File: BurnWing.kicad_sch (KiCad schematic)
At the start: 23 parts, among them J1 Molex_PicoBlade_53398-0471_1x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, J2 Molex_PicoBlade_53047-0610_1x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, J3 feather long, J4 feather short, U1 BTS3405GXUMA1, U3 AP63205WU-7

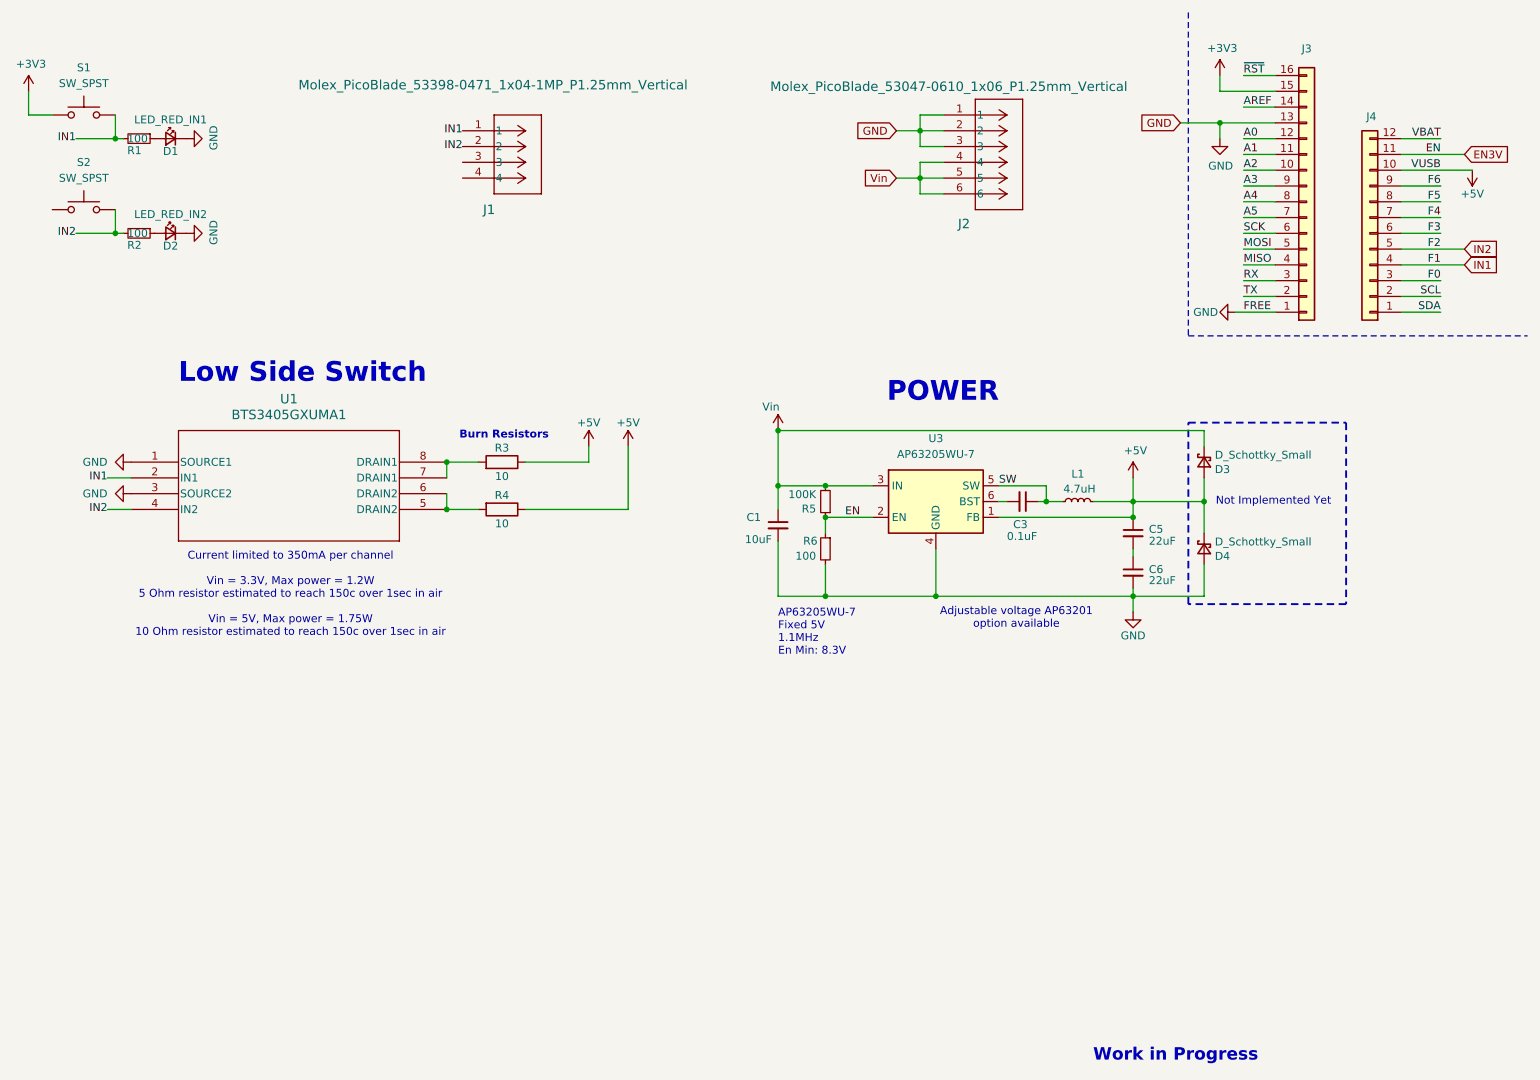
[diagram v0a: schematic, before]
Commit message: Layout adjustments + added diodes
Added some diodes to prevent backfeeding of test voltage.

Routed remaining two picoblade pins to EN pin on buck reg.
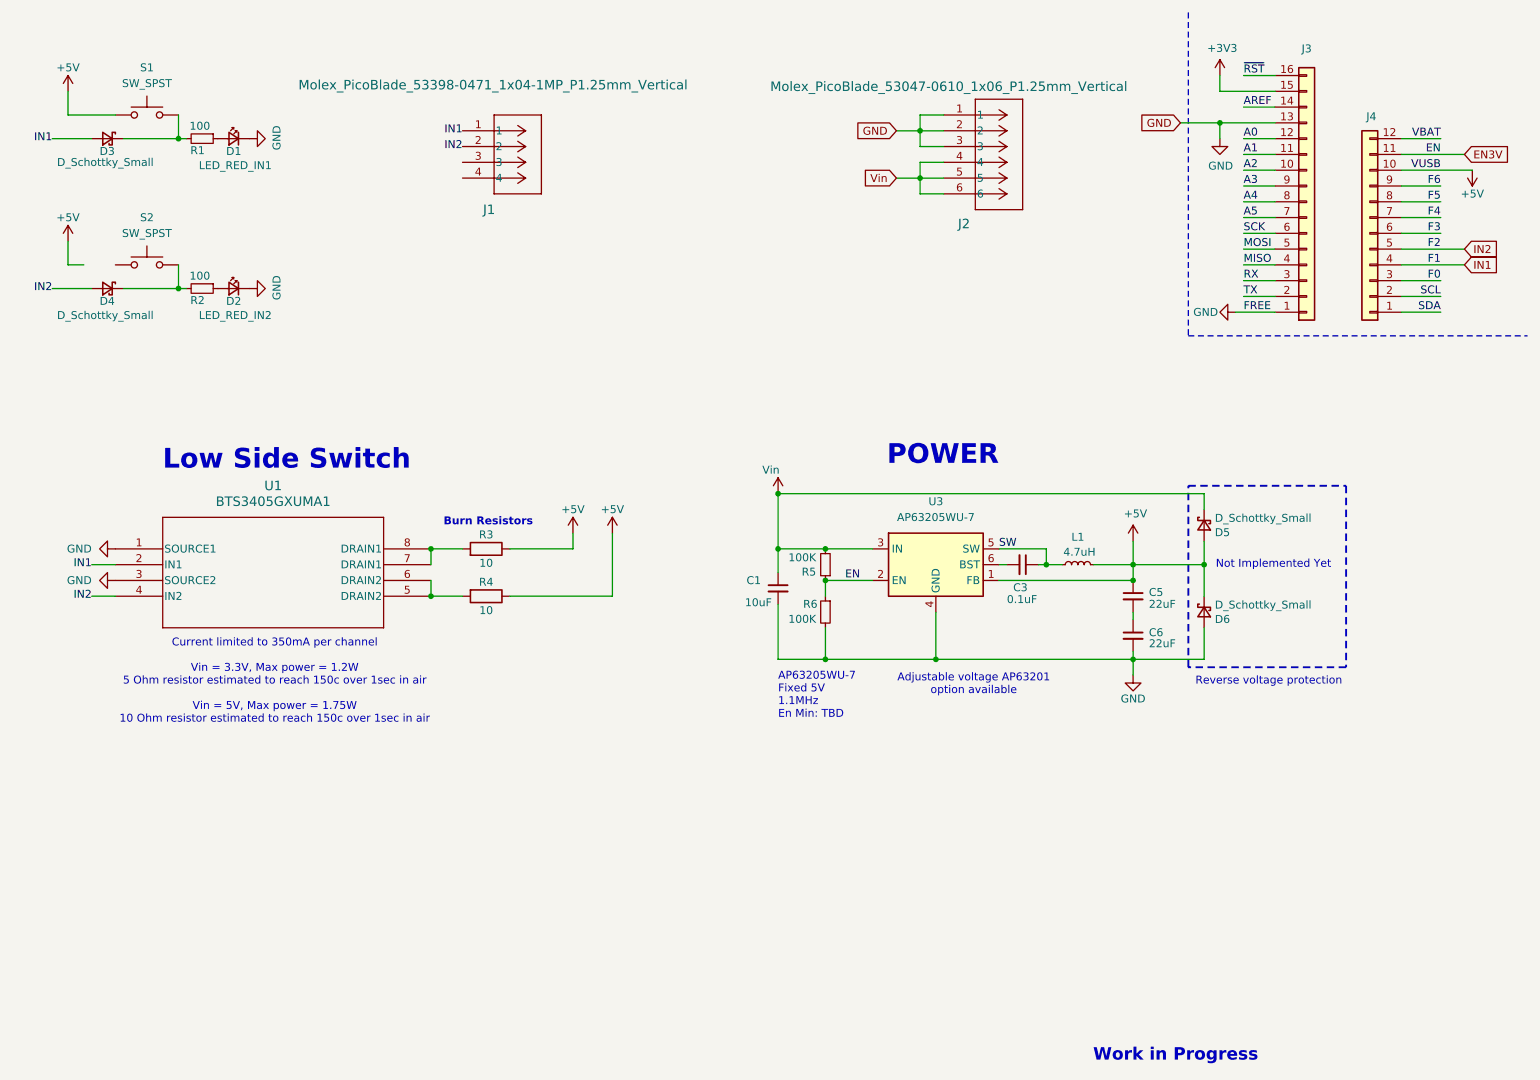
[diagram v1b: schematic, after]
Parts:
- added D3, D4: D_Schottky_Small, Diode_SMD:D_SOD-323, symbol Library:D_Schottky_Small
- R6: value 100 -> 100K
- renumbered D3 to D5, D4 to D6
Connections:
- net +3V3: no longer S1.1
- net +5V: now also S1.1
- net IN1: now also D3.2 (A); no longer R1.2, S1.2
- net IN2: now also D4.2 (A); no longer R2.2, S2.2
- new net: D3.1 (K), R1.2, S1.2
- new net: D4.1 (K), R2.2, S2.2
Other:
- note added: "AP63205WU-7 Fixed 5V 1.1MHz En Min: TBD"
- note added: "Reverse voltage protection"
- note removed: "AP63205WU-7 Fixed 5V 1.1MHz En Min: 8.3V"
- moved on the sheet: C1, C3, C5, C6, D1, D2, D5, D6, L1, R1, R2, R3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
